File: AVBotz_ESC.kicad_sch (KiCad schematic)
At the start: 30 parts, among them J1 Conn_01x04_Pin, J2 Conn_01x03_Pin, Q1 AO3404A, Q2 AO3404A, Q3 AO3404A, Q4 AO3404A, Q5 AO3404A, Q6 AO3404A, U1 ATtiny3227-M, U2 AP63205WU, U3 HIP2100_SOIC, U4 HIP2100_SOIC, U5 HIP2100_SOIC, U6 INA193, U7 INA193

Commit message: finalized
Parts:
- removed D1: SMAJ58A, PCM_SparkFun-Semiconductor-Standard:SMA, symbol PCM_SparkFun-DiscreteSemi:D_TVS_SMA_93.6V
- added C11, C12: 0.1uF, PCM_SparkFun-Capacitor:C_0402_1005Metric, symbol PCM_SparkFun-Capacitor:0.1uF_0402_16V_10%
- added D2: TVS, PCM_SparkFun-Semiconductor-Standard:SOT-363, symbol PCM_SparkFun-DiscreteSemi:D_TVS
- J1: footprint (none) -> PCM_SparkFun-Connector:JST_1x04_P1.0mm_Horizontal_SMD
- J2: footprint (none) -> PCM_SparkFun-Connector:JST_1x03_P1.0mm_Horizontal_SMD
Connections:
- net 12V: now also C11.1, C12.1, D2.1 (A1)
- net GND: now also C11.2, C12.2, D2.2 (A2)

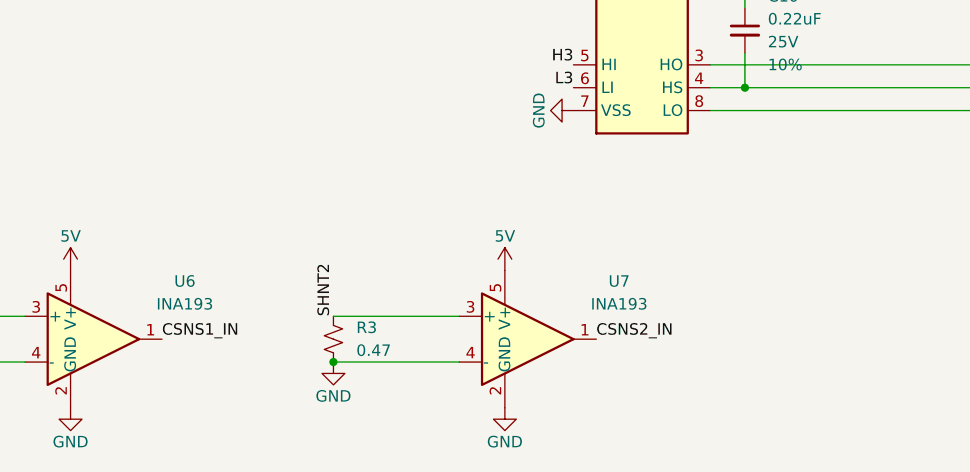
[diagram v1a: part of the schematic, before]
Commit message: rotate board & RC filters
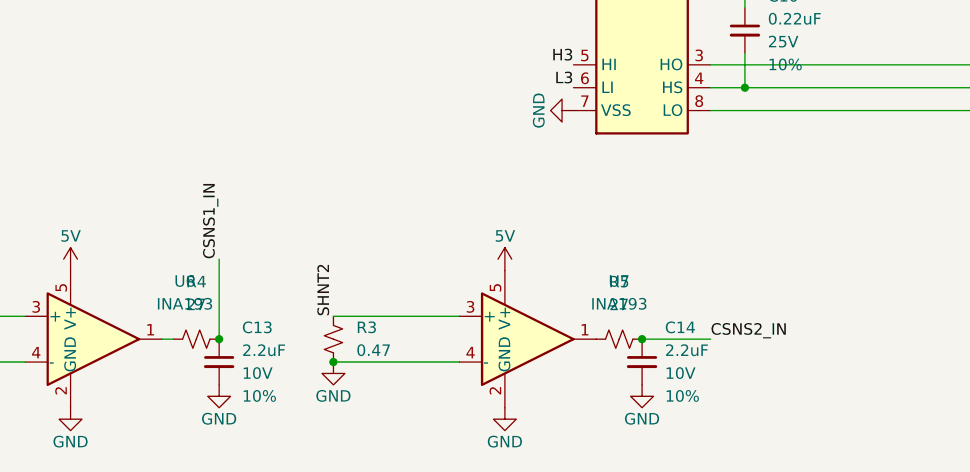
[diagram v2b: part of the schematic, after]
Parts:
- added C13, C14: 2.2uF, PCM_SparkFun-Capacitor:C_0402_1005Metric, symbol PCM_SparkFun-Capacitor:2.2uF_0402_10V_10%
- added R4, R5: 27, PCM_SparkFun-Resistor:R_0402_1005Metric, symbol PCM_SparkFun-Resistor:27_0402
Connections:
- net CSNS1_IN: now also C13.1, R4.2; no longer U6.1
- net CSNS2_IN: now also C14.1, R5.2; no longer U7.1
- net GND: now also C13.2, C14.2
- new net: R5.1, U7.1
- new net: R4.1, U6.1

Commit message: length matching
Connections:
- net CSD_B: now reaches R5.1, U7.1
- net CSD_A: now reaches R4.1, U6.1
- net CSNS1_IN renamed CSNS_A
- net CSNS_A: now also U1.8 (PA7); no longer U1.7 (PA6)
- net CSNS2_IN renamed CSNS_B
- net CSNS_B: now also U1.7 (PA6); no longer U1.8 (PA7)
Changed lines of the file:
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@@
-		)
-	)
-	(label "CSNS2_IN"
-		(at 118.11 93.98 0)
-		(effects
-			(font
-				(size 1.27 1.27)
-			)
-			(justify left bottom)
 		)
 	)
@@
 			)
 			(justify left bottom)
+		)
+	)
+	(label "CSNS_B"
+		(at 118.11 91.44 0)
+		(effects
+			(font
+				(size 1.27 1.27)
+			)
+			(justify left bottom)
+		)
+	)
+	(label "CSD_A"
+		(at 92.71 170.18 270)
+		(effects
+			(font
+				(size 1.27 1.27)
+			)
+			(justify right bottom)
 		)
 	)
@@
 		)
 	)
+	(label "CSD_B"
+		(at 140.97 170.18 270)
+		(effects
+			(font
+				(size 1.27 1.27)
+			)
+			(justify right bottom)
+		)
+	)
 	(label "UPDI"
 		(at 124.46 76.2 0)
@@
 		)
 	)
-	(label "CSNS2_IN"
+	(label "CSNS_B"
 		(at 153.67 170.18 0)
 		(effects
@@
 		)
 	)
-	(label "CSNS1_IN"
-		(at 118.11 91.44 0)
+	(label "CSNS_A"
+		(at 118.11 93.98 0)
 		(effects
 			(font
@@
 		)
 	)
-	(label "CSNS1_IN"
+	(label "CSNS_A"
 		(at 99.06 161.29 90)
 		(effects

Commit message: code + updates
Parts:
- added H1: MountingHole_Pad, MountingHole:MountingHole_2.2mm_M2_DIN965_Pad, symbol Mechanical:MountingHole_Pad
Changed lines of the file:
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@@
+	)
+	(symbol
+		(lib_id "Mechanical:MountingHole_Pad")
+		(at 196.85 43.18 0)
+		(unit 1)
+		(body_style 1)
+		(exclude_from_sim no)
+		(in_bom no)
+		(on_board yes)
+		(in_pos_files yes)
+		(dnp no)
+		(fields_autoplaced yes)
+		(property "Reference" "H1"
+			(at 199.39 40.6399 0)
+			(show_name no)
+			(do_not_autoplace no)
+			(effects
+				(font
+					(size 1.27 1.27)
+				)
+				(justify left)
+			)
+		)
+		(property "Value" "MountingHole_Pad"
+			(at 199.39 43.1799 0)
+			(show_name no)
+			(do_not_autoplace no)
+			(effects
+				(font
+					(size 1.27 1.27)
+				)
+				(justify left)
+			)
+		)
+		(property "Footprint" "MountingHole:MountingHole_2.2mm_M2_DIN965_Pad"
+			(at 196.85 43.18 0)
+			(hide yes)
+			(show_name no)
+			(do_not_autoplace no)
+			(effects
+				(font
+					(size 1.27 1.27)
+				)
+			)
+		)
+		(property "Datasheet" ""
+			(at 196.85 43.18 0)
+			(hide yes)
+			(show_name no)
+			(do_not_autoplace no)
+			(effects
+				(font
+					(size 1.27 1.27)
+				)
+			)
+		)
+		(property "Description" "Mounting Hole with connection"
+			(at 196.85 43.18 0)
+			(hide yes)
+			(show_name no)
+			(do_not_autoplace no)
+			(effects
+				(font
+					(size 1.27 1.27)
+				)
+			)
+		)
+		(pin "1"
+		)
+		(instances
+			(project "AVBotz_ESC"
+				(path "/40a7d472-403e-4671-a0c9-b27554a188a0"
+					(reference "H1")
+					(unit 1)
+				)
+			)
+		)
 	)
 	(symbol

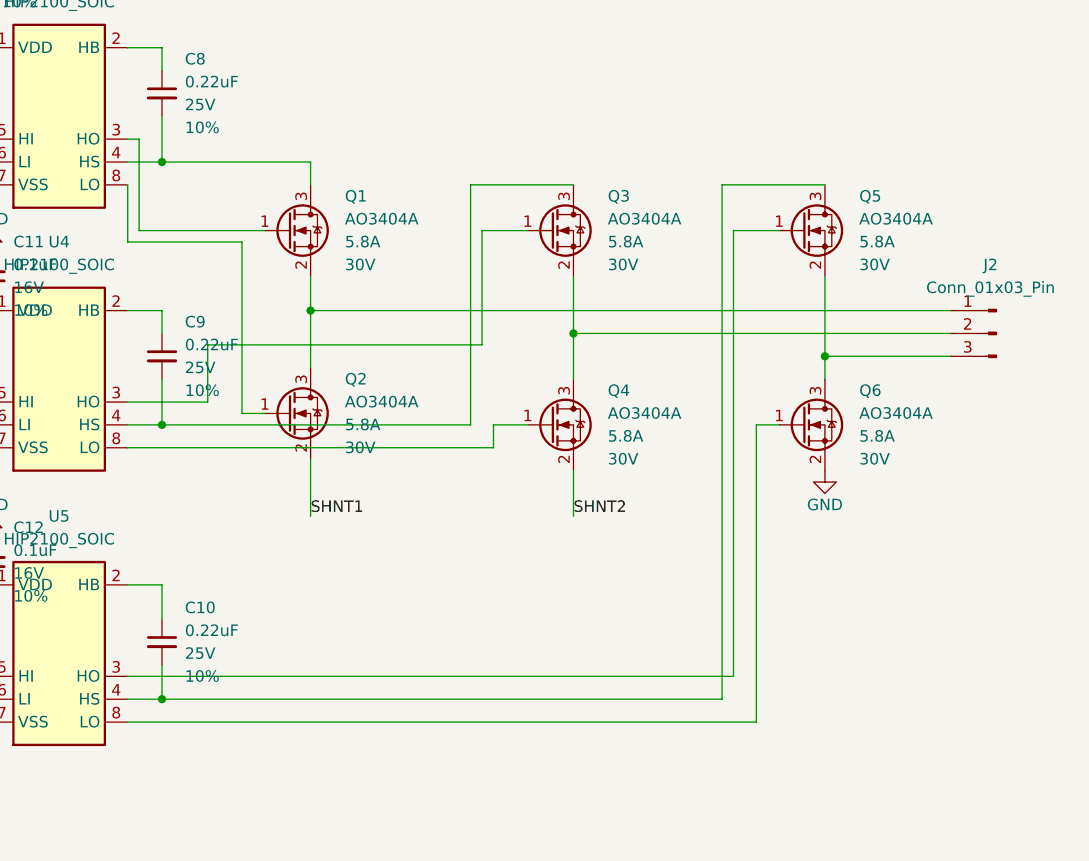
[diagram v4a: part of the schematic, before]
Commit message: update mosfet wiring
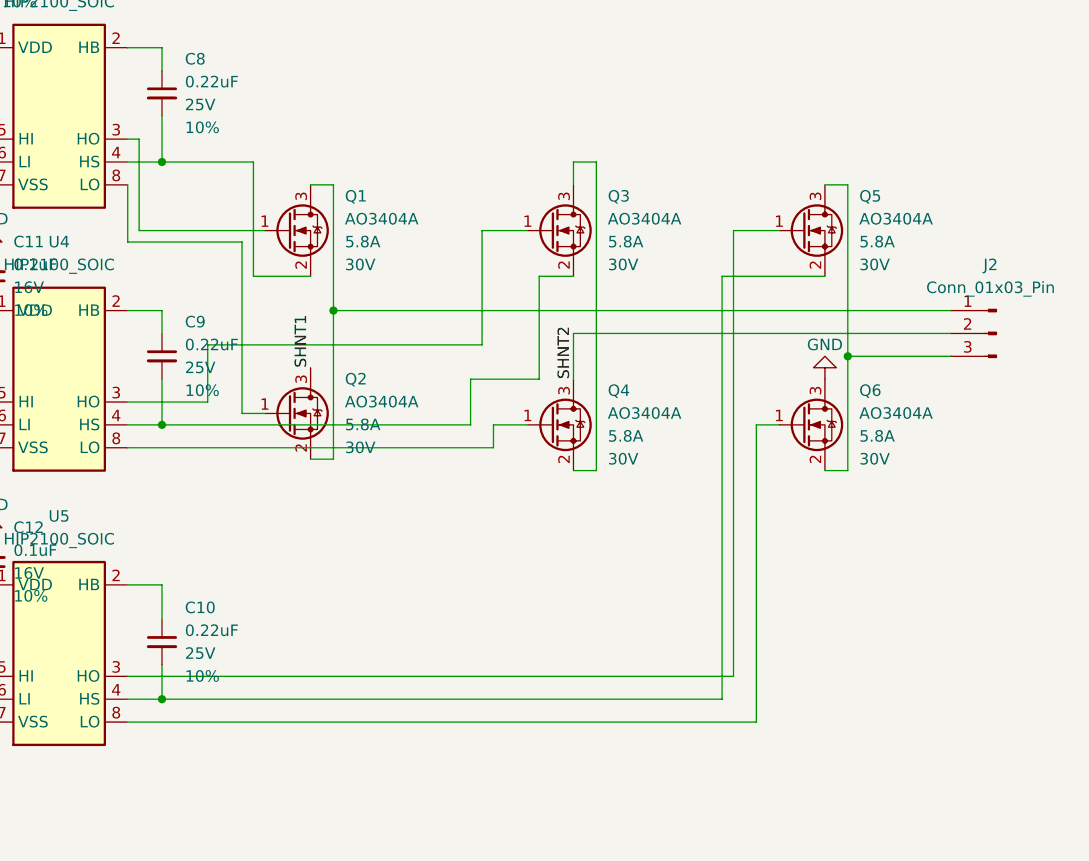
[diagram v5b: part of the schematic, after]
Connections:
- net GND: now also Q6.3 (D); no longer Q6.2 (S)
- net SHNT1: now also Q2.3 (D); no longer Q2.2 (S)
- net SHNT2: now also J2.2 (Pin_2), Q4.3 (D); no longer Q4.2 (S)
- net at C9.2, U4.4 (HS): now also Q3.2 (S); no longer Q3.3 (D)
- net at C10.2, U5.4 (HS): now also Q5.2 (S); no longer Q5.3 (D)
- net at C8.2, U3.4 (HS): now also Q1.2 (S); no longer Q1.3 (D)
- new net: Q3.3 (D), Q4.2 (S)
- new net: J2.3 (Pin_3), Q5.3 (D), Q6.2 (S)
- new net: J2.1 (Pin_1), Q1.3 (D), Q2.2 (S)
